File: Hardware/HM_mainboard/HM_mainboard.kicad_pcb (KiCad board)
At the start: 2 copper layers, 90 x 60 mm, 64 parts, among them J1 JST PH2P ST90, J2 USB4105-GF-A, J3 Conn_01x04, J4 54-00174, J5 54-00174, J6 54-00174, J7 54-00174, Q1 PMOS - AS3401, U1 MCP73831-2, U2 TC1262-33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

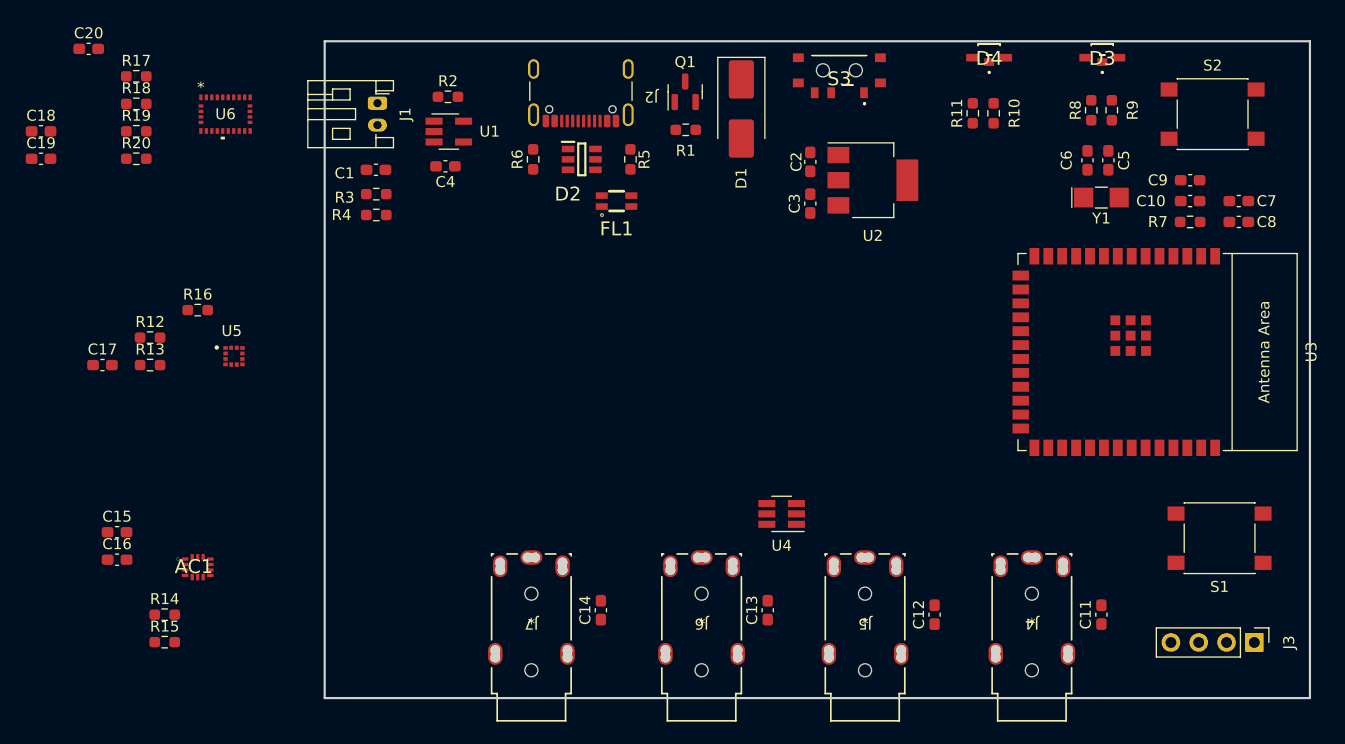
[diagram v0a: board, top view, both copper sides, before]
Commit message: Updated footprint of auxiliary jacks, routed first version of PCB
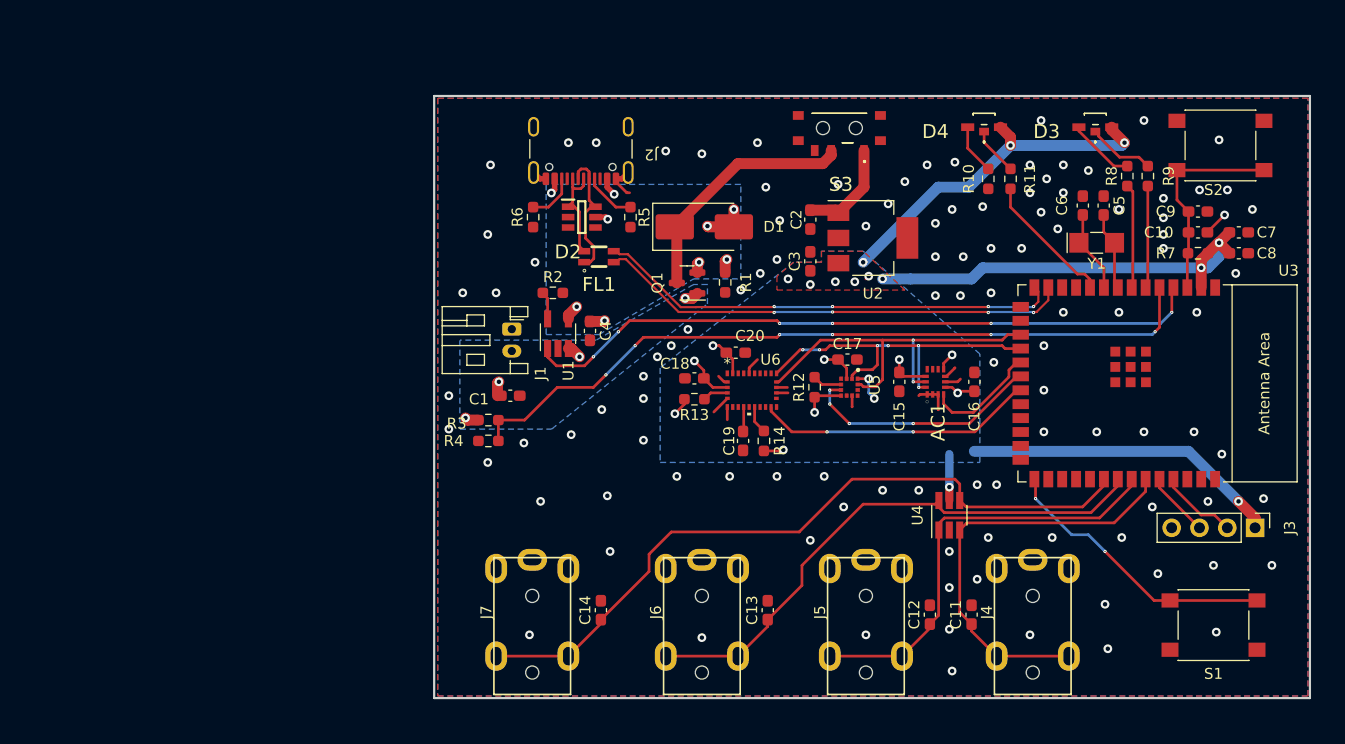
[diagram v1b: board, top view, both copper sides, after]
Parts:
- removed R15, R19, R20: 4.7k, Resistor_SMD:R_0603_1608Metric_Pad0.98x0.95mm_HandSolder
- removed R16, R17, R18: 10k, Resistor_SMD:R_0603_1608Metric_Pad0.98x0.95mm_HandSolder
- J4, J5, J6, J7: footprint HeadMouse:54-00174_TEN -> HeadMouse:54-00174
- R12, R13, R14: value 4.7k -> 10k
- moved C16 80.0 mm to (166.1, 99.1), turned to 90 degrees
- moved C15 72.8 mm to (159.3, 99.1), turned to -90 degrees
- moved AC1 69.5 mm to (162.6, 99.1), turned to 90 degrees
- moved C19 69.1 mm to (145.0, 104.5), turned to 90 degrees
- moved C17 68.1 mm to (154.5, 97.0)
- moved C20 65.3 mm to (144.3, 96.4)
- moved C18 63.8 mm to (140.5, 98.7), turned to 180 degrees
- moved R12 60.9 mm to (151.5, 99.6), turned to 90 degrees
- moved R14 57.0 mm to (146.9, 104.5), turned to -90 degrees
- moved U5 56.3 mm to (154.7, 99.6), turned to -90 degrees
- moved U6 54.3 mm to (145.8, 99.8)
- moved R13 49.8 mm to (140.5, 100.6), turned to 180 degrees
- moved C1 24.0 mm to (123.7, 100.3)
- moved J1 24.0 mm to (123.9, 94.2)
- moved R3 23.0 mm to (121.7, 102.6)
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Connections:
- R12 pad 2: /I2C_SCL -> Net-(U5-INTA)
- R13 pad 1: 3.3V -> Net-(U6-NBOOT_LOAD_PIN)
- R13 pad 2: /I2C_SDA -> 3.3V
- R14 pad 1: 3.3V -> Net-(U6-NRESET)
- R14 pad 2: /I2C_SDA -> 3.3V
- U3 pad 10: /Microcontroller - ESP32-S3-WROOM/GPIO_17 -> /LED_DEV_R
- U3 pad 11: /Microcontroller - ESP32-S3-WROOM/GPIO_18 -> /LED_DEV_G
- U3 pad 28: /LED_BAT_R -> /Microcontroller - ESP32-S3-WROOM/GPIO_35
- U3 pad 29: /LED_BAT_G -> /Microcontroller - ESP32-S3-WROOM/GPIO_36
- U3 pad 30: /LED_DEV_R -> /Microcontroller - ESP32-S3-WROOM/GPIO_37
- U3 pad 31: /LED_DEV_G -> /Microcontroller - ESP32-S3-WROOM/GPIO_38
- U3 pad 6: /Microcontroller - ESP32-S3-WROOM/GPIO_6 -> /LED_BAT_R
- U3 pad 7: /Microcontroller - ESP32-S3-WROOM/GPIO_7 -> /LED_BAT_G
- U4 pad 1: /BTN_1 -> /BTN_2
- U4 pad 3: /BTN_2 -> /BTN_1
- U4 pad 4: /BTN_3 -> /BTN_4
- U4 pad 6: /BTN_4 -> /BTN_3
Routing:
- net 3.3V: track 0.00 -> 133.7 mm, vias 0 -> 22
- net /V_BATT_MEASURE: track 0.00 -> 69.4 mm, vias 0 -> 6
- net /BTN_4: track 0.00 -> 66.7 mm
- net /BATT_CHARGING_STATUS: track 0.00 -> 62.7 mm, vias 0 -> 6
- net /BTN_3: track 0.00 -> 51.1 mm
- net /Microcontroller - ESP32-S3-WROOM/USB_C_D-: track 0.00 -> 43.5 mm, vias 0 -> 4
- net /Microcontroller - ESP32-S3-WROOM/USB_C_D+: track 0.00 -> 42.7 mm, vias 0 -> 4
- net /BTN_2: track 0.00 -> 39.8 mm
- net /BTN_1: track 0.00 -> 39.1 mm
- net /I2C_SCL: track 0.00 -> 35.3 mm, vias 0 -> 2
- net /I2C_SDA: track 0.00 -> 32.7 mm, vias 0 -> 6
- net /Microcontroller - ESP32-S3-WROOM/BOOT: track 0.00 -> 25.9 mm, vias 0 -> 2
- net GND: track 0.00 -> 25.8 mm, vias 0 -> 112
- net /BNO55_INT: track 0.00 -> 25.5 mm, vias 0 -> 2
- net /Battery_and_Power_Managment/V_PWR_SWITCH: track 0.00 -> 22.6 mm
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- added copper zone on B.Cu, net 3.3V
- added copper zone on F.Cu, net 3.3V
- added copper zone on B.Cu, net GND
- added copper zone on F.Cu, net GND
- added copper zone on B.Cu, net V_BATT
- added copper zone on B.Cu, net V_USB
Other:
- board size 90 x 60 mm -> 80 x 55 mm

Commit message: Added BOM
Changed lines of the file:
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@@
       (outputformat 1)
       (mirror false)
-      (drillshape 1)
+      (drillshape 0)
       (scaleselection 1)
       (outputdirectory "")
@@
     (fp_line (start 3.95 6.25) (end 3.95 -1.35)
       (stroke (width 0.1) (type solid)) (layer "F.Fab"))
-    (pad "1" thru_hole roundrect (at 0 0 270) (size 1.2 1.75) (drill 0.75) (layers "*.Cu" "*.Mask") (roundrect_rratio 0.208333)
+    (pad "1" thru_hole roundrect (at 0 0 270) (size 1.2 1.75) (drill 0.75) (layers "*.Cu" "*.Mask") (roundrect_rratio 0.2083333333)
       (net 1 "GND") (pinfunction "Pin_1") (pintype "passive"))
     (pad "2" thru_hole oval (at 2 0 270) (size 1.2 1.75) (drill 0.75) (layers "*.Cu" "*.Mask")

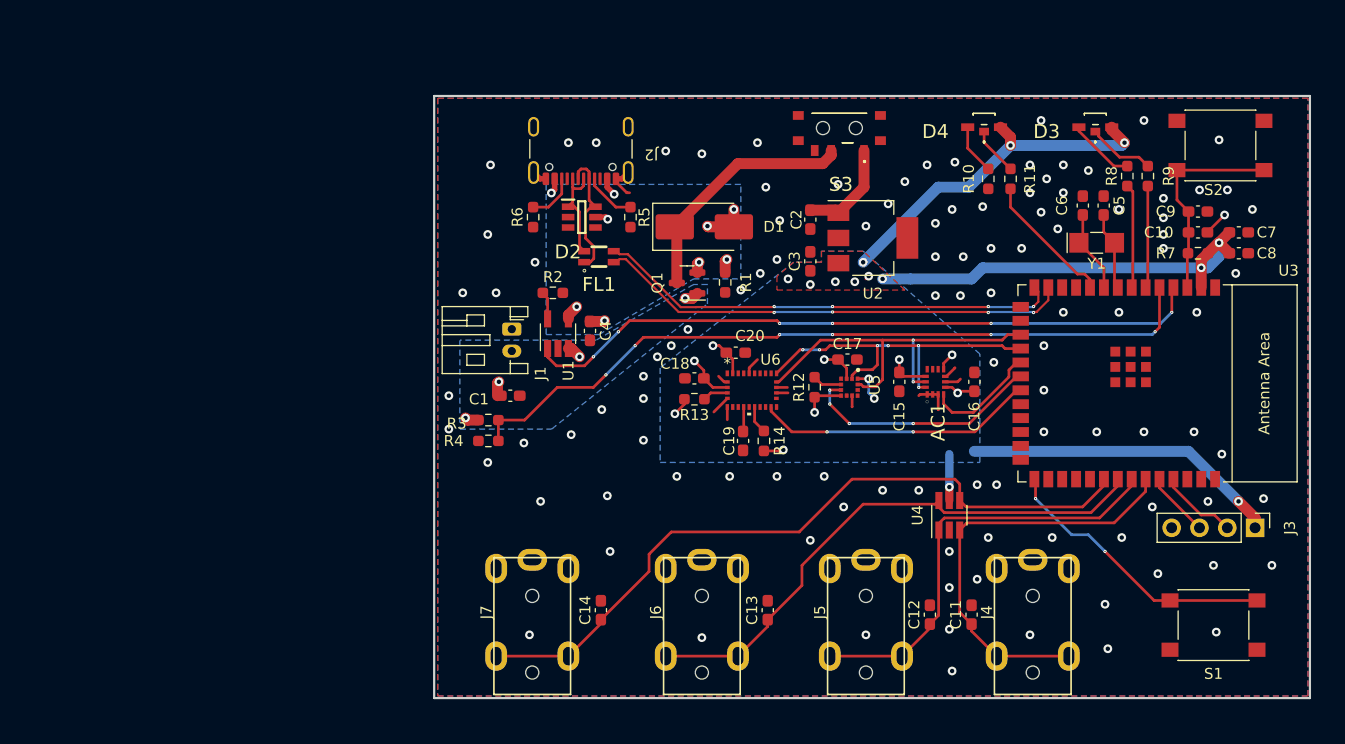
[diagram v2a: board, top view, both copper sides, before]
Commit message: Moved measurement lines. Updated PCB according to Aisler DRC
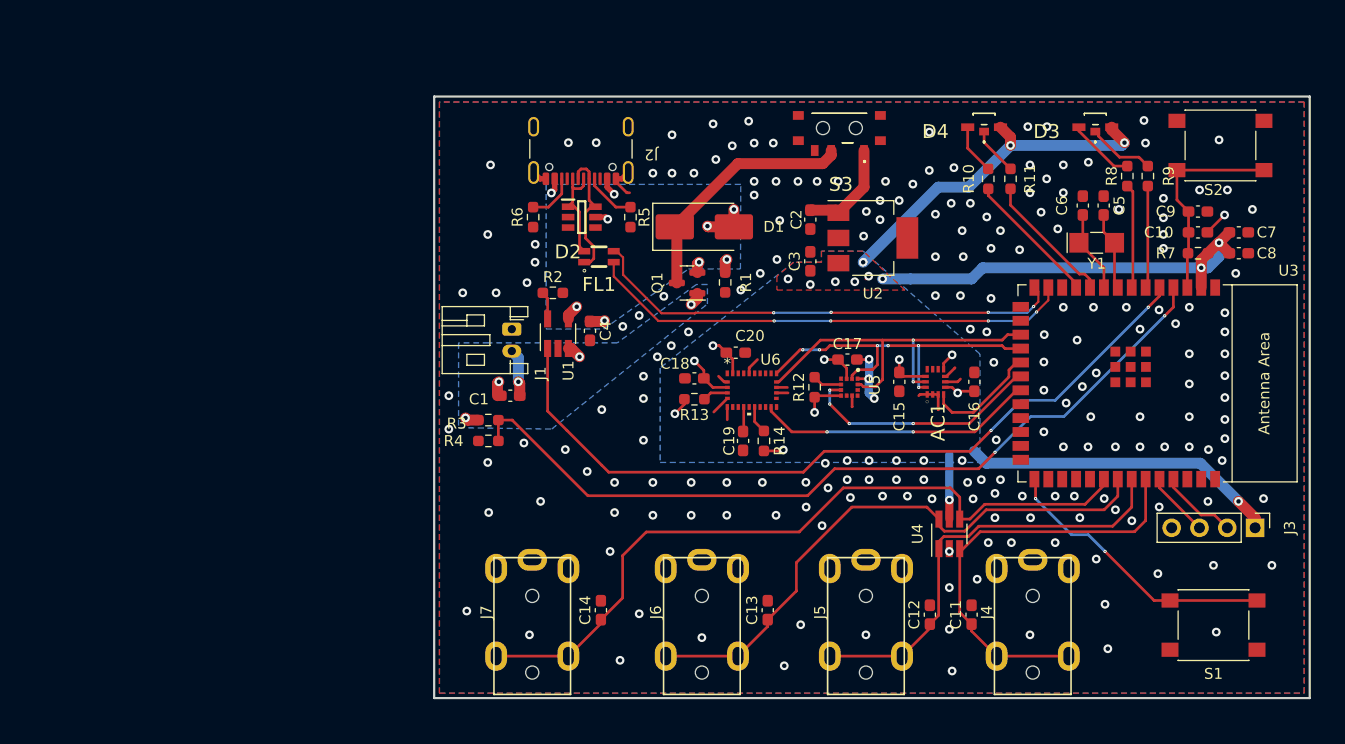
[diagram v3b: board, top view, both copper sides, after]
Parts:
- C1, C4: value 4.7u -> 4.7uF
- C10, C19: value 1uF -> 1.0uF-25V-(+80/-20%)
- C11, C12, C13, C14: value 100n -> 100nF
- C15, C16, C17: value 0.1uF -> 100nF
- C2, C3: value 1.0UF-25V-(+80/-20%) -> 1.0uF-25V-(+80/-20%)
- C20: value 120nF -> 100nF
- moved U4 1.70 mm to (163.8, 113.0)
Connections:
- U3 pad 4: /BATT_CHARGING_STATUS -> /V_BATT_MEASURE
- U3 pad 5: /V_BATT_MEASURE -> /BATT_CHARGING_STATUS
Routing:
- net /LED_DEV_G: track 0.00 -> 12.3 mm
- net /BATT_CHARGING_STATUS: track 62.7 -> 71.4 mm, vias 6 -> 2
- net /V_BATT_MEASURE: track 69.4 -> 75.4 mm, vias 6 -> 2
- net V_BATT: track 3.89 -> 8.22 mm, vias 3 -> 4
- net GND: track 25.8 -> 28.7 mm, vias 112 -> 206
- net /BTN_3: track 51.1 -> 53.0 mm
- net /BTN_4: track 66.7 -> 68.6 mm
- net 3.3V: track 133.7 -> 135.4 mm
- net /Microcontroller - ESP32-S3-WROOM/USB_C_D+: track 42.7 -> 44.0 mm
- net /Microcontroller - ESP32-S3-WROOM/USB_C_D-: track 43.5 -> 44.6 mm
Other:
- board text added: "HeadMouse V1.0 FH Technikum Wien"

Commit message: Updated BOM
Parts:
- moved C4 2.12 mm to (132.8, 93.4)
- moved J1 2.12 mm to (125.7, 93.2)
- moved R3 2.12 mm to (123.6, 101.5)
- moved U1 2.12 mm to (129.9, 93.6)
- moved C1 2.12 mm to (125.6, 99.3)
- moved R4 2.12 mm to (123.6, 103.4)
- moved R2 1.56 mm to (127.0, 89.5), turned to 0 degrees
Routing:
- net /V_BATT_MEASURE: track 75.4 -> 73.2 mm
- net GND: track 28.7 -> 30.7 mm, vias 206 -> 228
- net Net-(U1-PROG): track 2.35 -> 3.20 mm
- net /Microcontroller - ESP32-S3-WROOM/USB_C_D-: track 44.6 -> 45.5 mm
- net /Microcontroller - ESP32-S3-WROOM/USB_C_D+: track 44.0 -> 44.8 mm
- net V_BATT: track 8.22 -> 9.00 mm
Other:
- outline, holes or cut-outs redrawn

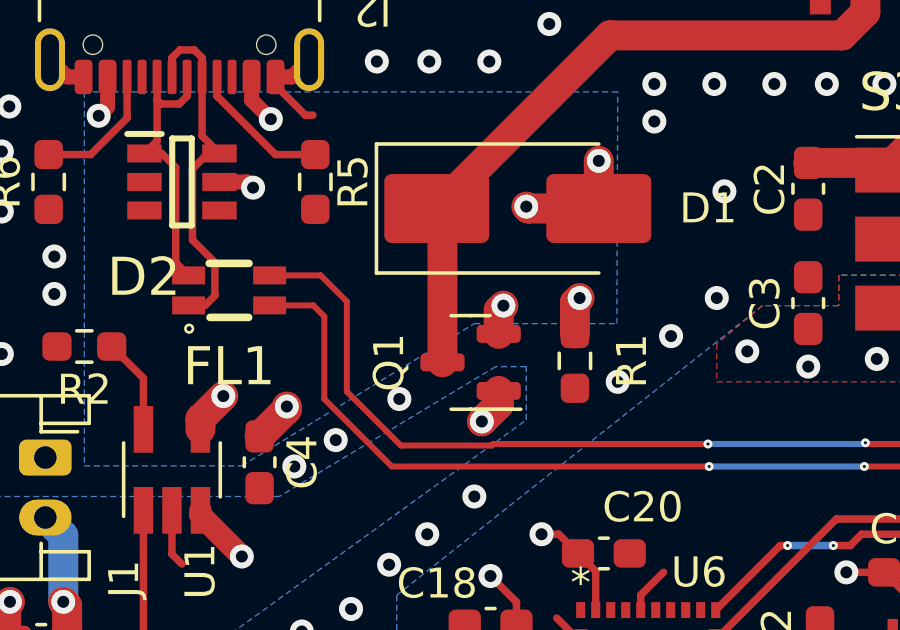
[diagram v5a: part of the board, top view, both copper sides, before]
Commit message: Fixed wrong symbol-to-footprint assignment of PMOS AS3401
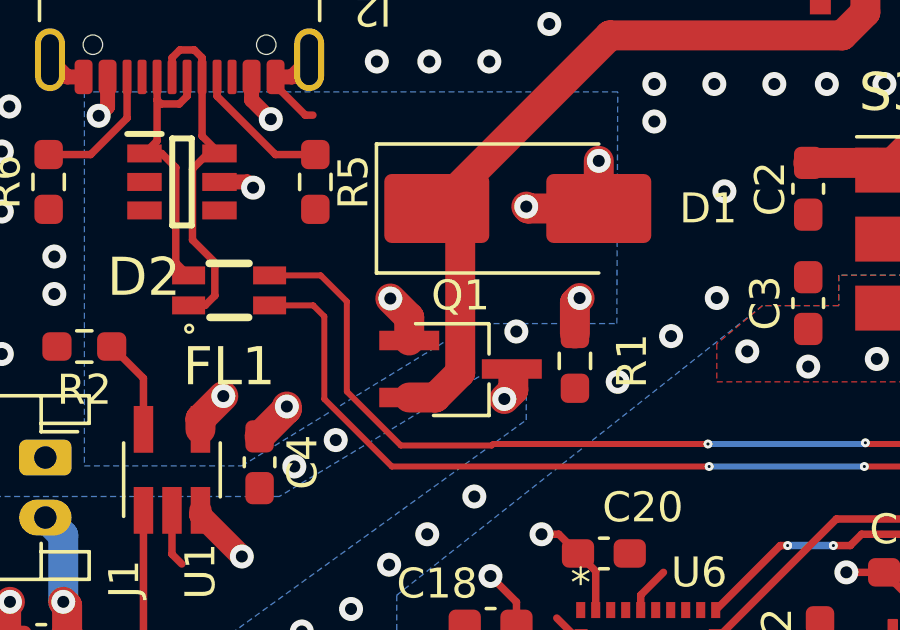
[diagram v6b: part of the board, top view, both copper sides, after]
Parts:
- Q1: value PMOS - AS3401 -> PMOS AS3401; footprint Package_TO_SOT_SMD:SOT-23 -> Package_TO_SOT_SMD:TSOT-23_HandSoldering
- moved Q1 0.40 mm to (139.5, 90.2), turned to 0 degrees
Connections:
- Q1 pad 1: V_BATT -> V_USB
- Q1 pad 2: V_USB -> /Battery_and_Power_Managment/V_PWR_SWITCH
- Q1 pad 3: /Battery_and_Power_Managment/V_PWR_SWITCH -> V_BATT
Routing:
- net /Battery_and_Power_Managment/V_PWR_SWITCH: track 22.6 -> 25.5 mm
- net V_USB: track 13.9 -> 14.5 mm

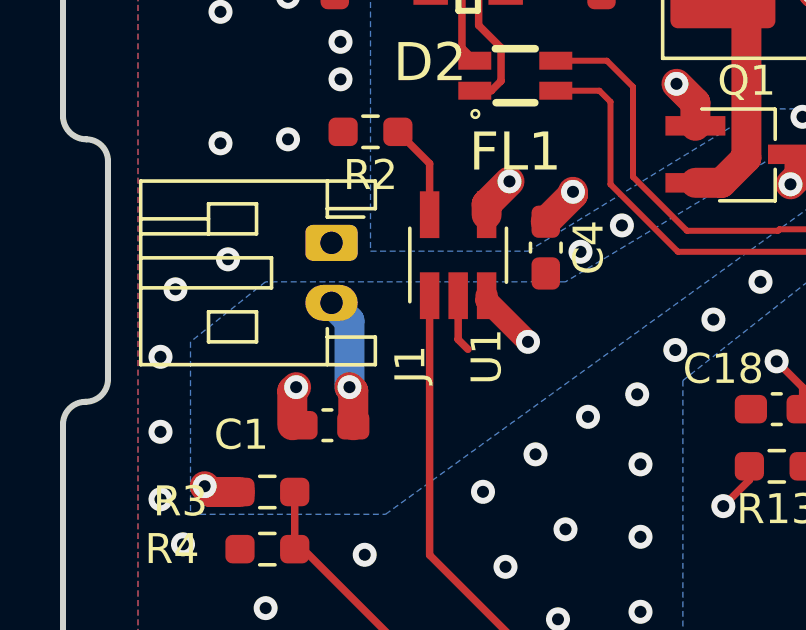
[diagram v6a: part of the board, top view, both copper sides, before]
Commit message: Swapped battery polarity due to wrong pinning assumption
Bugfix
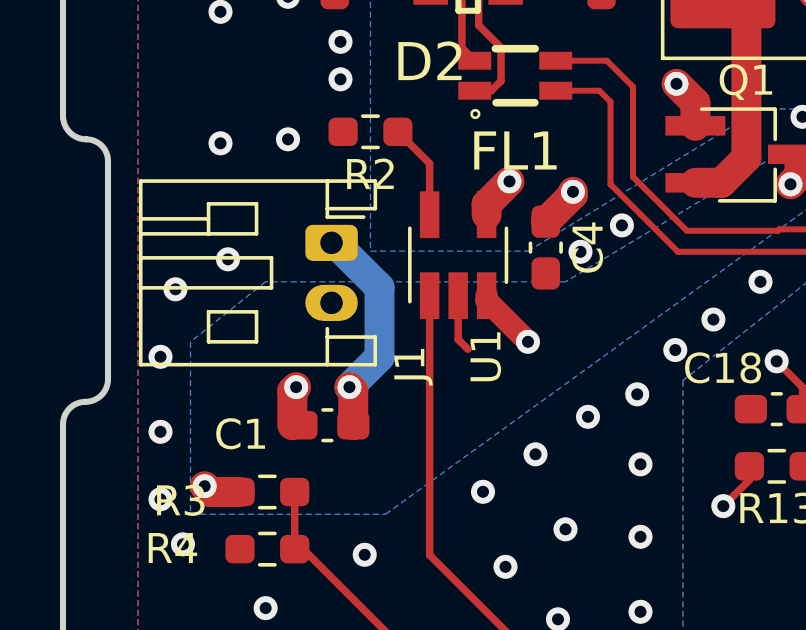
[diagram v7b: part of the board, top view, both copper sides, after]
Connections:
- J1 pad 1: GND -> V_BATT
- J1 pad 2: V_BATT -> GND
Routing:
- net V_BATT: track 8.52 -> 11.4 mm
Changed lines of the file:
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@@
       (stroke (width 0.1) (type solid)) (layer "F.Fab"))
     (pad "1" thru_hole roundrect (at 0 0 270) (size 1.2 1.75) (drill 0.75) (layers "*.Cu" "*.Mask") (roundrect_rratio 0.2083333333)
-      (net 1 "GND") (pinfunction "Pin_1") (pintype "passive"))
+      (net 11 "V_BATT") (pinfunction "Pin_1") (pintype "passive"))
     (pad "2" thru_hole oval (at 2 0 270) (size 1.2 1.75) (drill 0.75) (layers "*.Cu" "*.Mask")
-      (net 11 "V_BATT") (pinfunction "Pin_2") (pintype "passive"))
+      (net 1 "GND") (pinfunction "Pin_2") (pintype "passive"))
     (model "${KICAD6_3DMODEL_DIR}/Connector_JST.3dshapes/JST_PH_S2B-PH-K_1x02_P2.00mm_Horizontal.wrl"
       (offset (xyz 0 0 0))
@@
   (via (at 121.473 101.313) (size 0.8) (drill 0.4) (layers "F.Cu" "B.Cu") (net 11))
   (via (at 141 91.25) (size 0.8) (drill 0.4) (layers "F.Cu" "B.Cu") (net 11))
-  (segment (start 126.299 95.799) (end 125.701 95.201) (width 1) (layer "B.Cu") (net 11))
-  (segment (start 126.299 98.011) (end 126.299 95.799) (width 1) (layer "B.Cu") (net 11))
+  (segment (start 127.3 94.686522) (end 125.814478 93.201) (width 1) (layer "B.Cu") (net 11))
+  (segment (start 125.814478 93.201) (end 125.701 93.201) (width 1) (layer "B.Cu") (net 11))
+  (segment (start 126.299 98.011) (end 127.3 97.01) (width 1) (layer "B.Cu") (net 11))
+  (segment (start 127.3 97.01) (end 127.3 94.686522) (width 1) (layer "B.Cu") (net 11))
   (segment (start 178.917 90.147) (end 179.22 90.45) (width 0.25) (layer "F.Cu") (net 12))
   (segment (start 177.927 85.37) (end 178.917 86.36) (width 0.25) (layer "F.Cu") (net 12))
